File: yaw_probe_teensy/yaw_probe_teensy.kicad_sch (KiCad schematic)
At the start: 5 parts, among them J1 Conn_01x04_Female, U1 Teensy4.0, U2 MS4525DO, U3 MS4525DO, U4 SN65HVD230_CAN_Transceiver

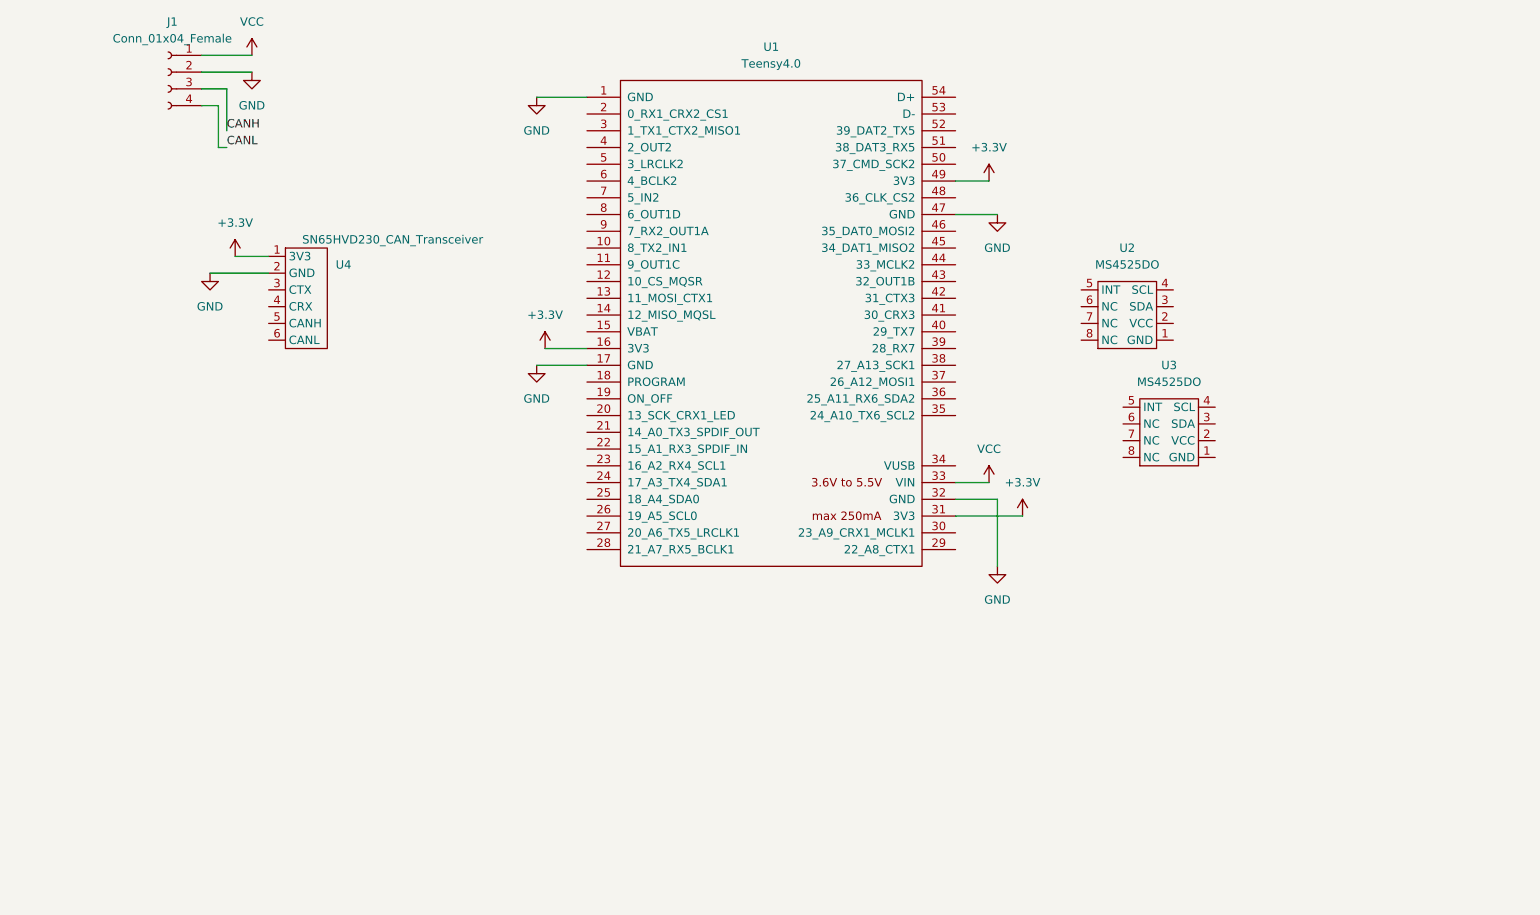
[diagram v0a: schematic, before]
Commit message: yaw probe teensy: schematic finished
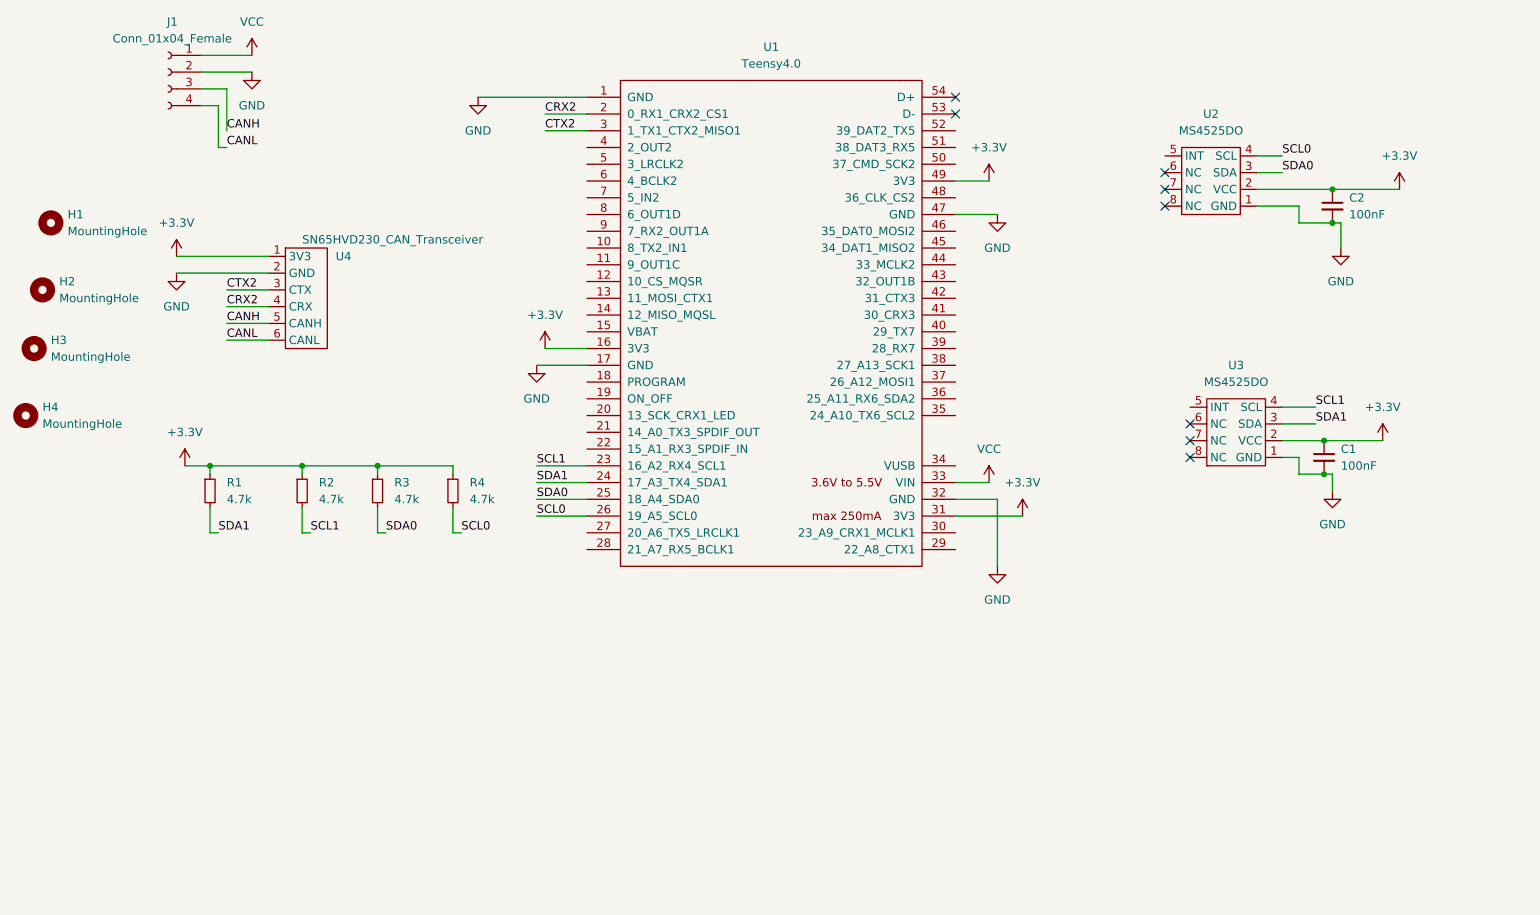
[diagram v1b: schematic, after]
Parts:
- added C1, C2: 100nF, symbol Device:C_Small
- added H1, H2, H3, H4: MountingHole, symbol Mechanical:MountingHole
- added R1, R2, R3, R4: 4.7k, symbol Device:R_Small
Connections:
- net +3.3V: now also U2.2 (VCC), U3.2 (VCC), C1.1, C2.1, R1.1, R2.1, R3.1, R4.1
- net CANH: now also U4.5 (CANH)
- net CANL: now also U4.6 (CANL)
- net GND: now also U2.1 (GND), U3.1 (GND), C1.2, C2.2
- net SDA1: now reaches U3.3 (SDA)
- net SDA1: now also U1.24 (17_A3_TX4_SDA1), R1.2
- net SCL1: now reaches U3.4 (SCL)
- net SCL1: now also U1.23 (16_A2_RX4_SCL1), R2.2
- net CTX2: now reaches U4.3 (CTX)
- net CTX2: now also U1.3 (1_TX1_CTX2_MISO1)
- net CRX2: now reaches U4.4 (CRX)
- net CRX2: now also U1.2 (0_RX1_CRX2_CS1)
- net SDA0: now reaches U1.25 (18_A4_SDA0)
- net SDA0: now also U2.3 (SDA), R3.2
- net SCL0: now reaches U1.26 (19_A5_SCL0)
- net SCL0: now also U2.4 (SCL), R4.2
- no-connect marks 0 -> 8
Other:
- title: SDM-22 Yaw Probe -> SDM-23 Yaw Probe
- moved on the sheet: U2, U3

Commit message: started stm32 variant for yaw probe
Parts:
- H1, H2, H3, H4: footprint (none) -> MountingHole:MountingHole_3.2mm_M3
- J1: footprint (none) -> SDM:Binder_IP40_711_THT_4C
- U1: footprint (none) -> Teensy:Teensy40_SMT
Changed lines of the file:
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@@
       (effects (font (size 1.27 1.27)) (justify left))
     )
-    (property "Footprint" "" (id 2) (at 34.29 96.52 0)
+    (property "Footprint" "MountingHole:MountingHole_3.2mm_M3" (id 2) (at 34.29 96.52 0)
       (effects (font (size 1.27 1.27)) hide)
     )
@@
       (effects (font (size 1.27 1.27)) (justify left))
     )
-    (property "Footprint" "" (id 2) (at 35.56 86.36 0)
+    (property "Footprint" "MountingHole:MountingHole_3.2mm_M3" (id 2) (at 35.56 86.36 0)
       (effects (font (size 1.27 1.27)) hide)
     )
@@
       (effects (font (size 1.27 1.27)) (justify left))
     )
-    (property "Footprint" "" (id 2) (at 38.1 67.31 0)
+    (property "Footprint" "MountingHole:MountingHole_3.2mm_M3" (id 2) (at 38.1 67.31 0)
       (effects (font (size 1.27 1.27)) hide)
     )
@@
       (effects (font (size 1.27 1.27)) (justify left))
     )
-    (property "Footprint" "" (id 2) (at 36.83 77.47 0)
+    (property "Footprint" "MountingHole:MountingHole_3.2mm_M3" (id 2) (at 36.83 77.47 0)
       (effects (font (size 1.27 1.27)) hide)
     )
@@
     (property "Reference" "U1" (id 0) (at 147.32 40.64 0))
     (property "Value" "Teensy4.0" (id 1) (at 147.32 43.18 0))
-    (property "Footprint" "" (id 2) (at 137.16 77.47 0)
+    (property "Footprint" "Teensy:Teensy40_SMT" (id 2) (at 137.16 77.47 0)
       (effects (font (size 1.27 1.27)) hide)
     )
@@
     (property "Reference" "J1" (id 0) (at 56.515 36.83 0))
     (property "Value" "Conn_01x04_Female" (id 1) (at 56.515 39.37 0))
-    (property "Footprint" "" (id 2) (at 55.88 44.45 0)
+    (property "Footprint" "SDM:Binder_IP40_711_THT_4C" (id 2) (at 55.88 44.45 0)
       (effects (font (size 1.27 1.27)) hide)
     )
@@
     )
     (path "/8a11ec2b-d5aa-47fc-b55f-2d7715947a31"
-      (reference "H1") (unit 1) (value "MountingHole") (footprint "")
+      (reference "H1") (unit 1) (value "MountingHole") (footprint "MountingHole:MountingHole_3.2mm_M3")
     )
     (path "/a373a51e-6720-4ebf-be15-7f9cdf4ec4b8"
-      (reference "H2") (unit 1) (value "MountingHole") (footprint "")
+      (reference "H2") (unit 1) (value "MountingHole") (footprint "MountingHole:MountingHole_3.2mm_M3")
     )
     (path "/648b5334-9144-433b-8f9b-4b34383fde3a"
-      (reference "H3") (unit 1) (value "MountingHole") (footprint "")
+      (reference "H3") (unit 1) (value "MountingHole") (footprint "MountingHole:MountingHole_3.2mm_M3")
     )
     (path "/5040622c-3a41-491b-b35b-845caaa0a1f2"
-      (reference "H4") (unit 1) (value "MountingHole") (footprint "")
+      (reference "H4") (unit 1) (value "MountingHole") (footprint "MountingHole:MountingHole_3.2mm_M3")
     )
     (path "/e1059838-0c71-4301-a5b7-3b9d105e9284"
-      (reference "J1") (unit 1) (value "Conn_01x04_Female") (footprint "")
+      (reference "J1") (unit 1) (value "Conn_01x04_Female") (footprint "SDM:Binder_IP40_711_THT_4C")
     )
     (path "/8fca02e5-2732-483b-ad1a-a78a92441fab"
@@
     )
     (path "/b6059556-dcb7-4cd5-903e-0e6be7253ec2"
-      (reference "U1") (unit 1) (value "Teensy4.0") (footprint "")
+      (reference "U1") (unit 1) (value "Teensy4.0") (footprint "Teensy:Teensy40_SMT")
     )
     (path "/e78ea3f6-7e86-4790-9de6-8dee68503fda"

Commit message: imu box
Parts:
- C1, C2: footprint (none) -> Capacitor_THT:C_Disc_D3.0mm_W1.6mm_P2.50mm
- J1: footprint SDM:Binder_IP40_711_THT_4C -> TerminalBlock_TE-Connectivity:TerminalBlock_TE_282834-4_1x04_P2.54mm_Horizontal
- R1, R2, R3, R4: footprint (none) -> Resistor_THT:R_Axial_DIN0207_L6.3mm_D2.5mm_P7.62mm_Horizontal
- U1: footprint Teensy:Teensy40_SMT -> Teensy:Teensy40
- U2, U3: footprint (none) -> SDM:MS4525-DSvoxxxyP
- U4: footprint (none) -> SDM:SDM_CANBoard_v1
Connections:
- net +3.3V: now also U4.3 (3V3); no longer U1.16 (3V3), U1.49 (3V3), U4.1 (3V3)
- net CTX2: now also U4.1 (CTX); no longer U4.3 (CTX)
- net GND: no longer U1.17 (GND), U1.47 (GND)
- no-connect marks 8 -> 52
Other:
- company: Sun Devil Motorsports - Data Acquisition -> Sun Devil Motorsports
- moved on the sheet: H1, H2, H3, H4, R1, R2, R3, R4

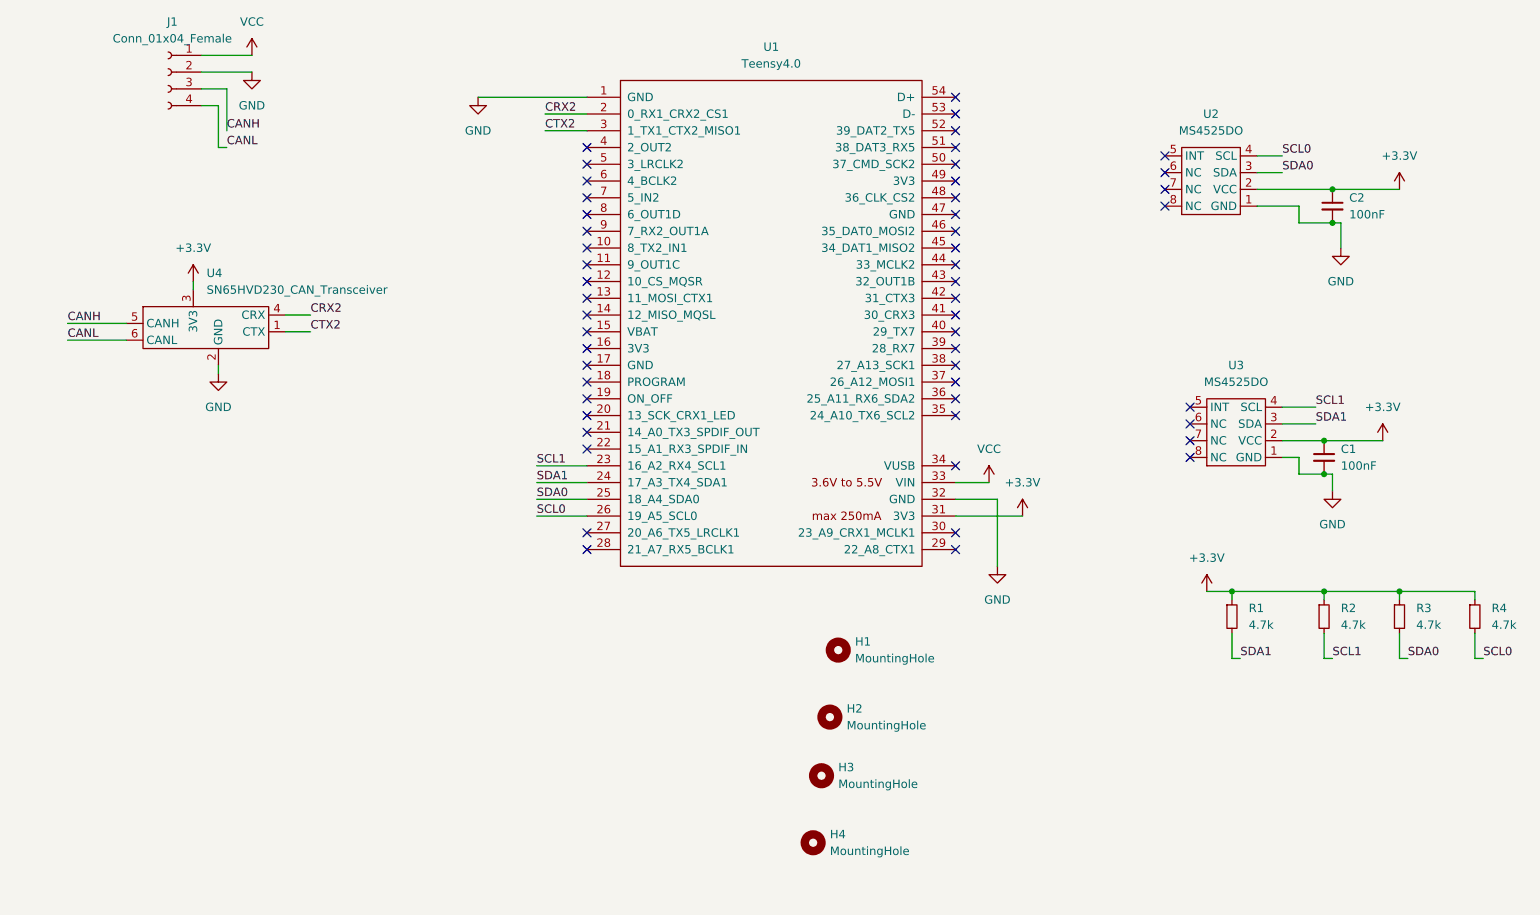
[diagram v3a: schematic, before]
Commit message: update yaw probe for DRS
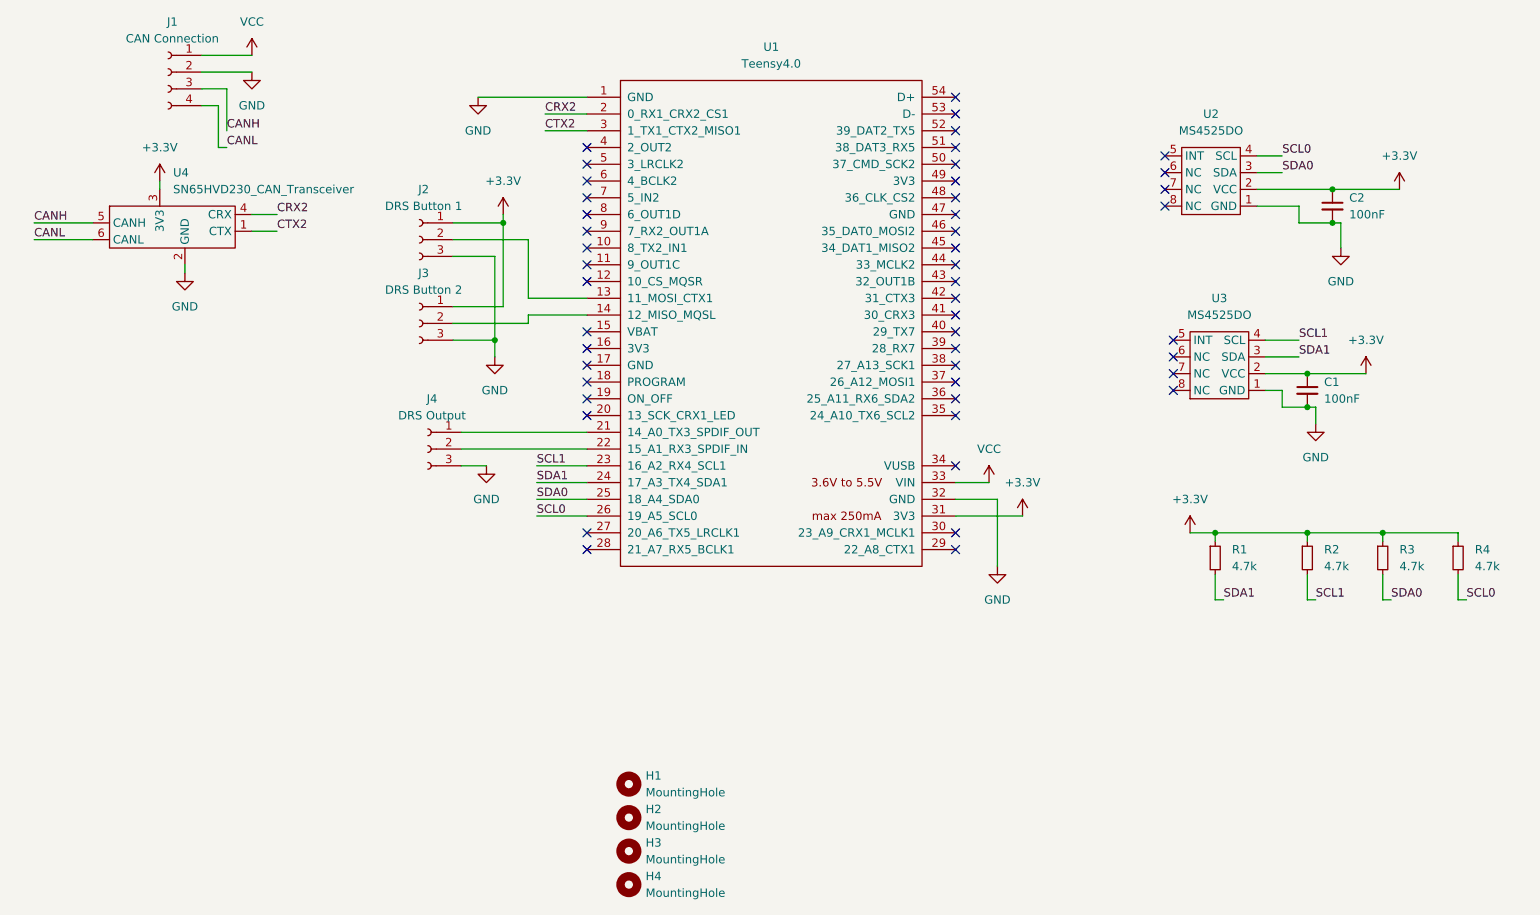
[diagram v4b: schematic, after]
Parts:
- added J2: DRS Button 1, TerminalBlock_TE-Connectivity:TerminalBlock_TE_282834-3_1x03_P2.54mm_Horizontal, symbol Connector:Conn_01x03_Female
- added J3: DRS Button 2, TerminalBlock_TE-Connectivity:TerminalBlock_TE_282834-3_1x03_P2.54mm_Horizontal, symbol Connector:Conn_01x03_Female
- added J4: DRS Output, TerminalBlock_TE-Connectivity:TerminalBlock_TE_282834-3_1x03_P2.54mm_Horizontal, symbol Connector:Conn_01x03_Female
- J1: value Conn_01x04_Female -> CAN Connection
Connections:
- net +3.3V: now also J2.1 (Pin_1), J3.1 (Pin_1)
- net GND: now also J2.3 (Pin_3), J3.3 (Pin_3), J4.3 (Pin_3)
- net at U1.13 (11_MOSI_CTX1): now also J2.2 (Pin_2)
- net at U1.14 (12_MISO_MQSL): now also J3.2 (Pin_2)
- net at U1.21 (14_A0_TX3_SPDIF_OUT): now also J4.1 (Pin_1)
- net at U1.22 (15_A1_RX3_SPDIF_IN): now also J4.2 (Pin_2)
- no-connect marks 52 -> 48
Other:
- moved on the sheet: C1, H1, H2, H3, H4, R1, R2, R3, R4, U3, U4

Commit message: silkscreen additions
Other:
- title: SDM-23 Yaw Probe -> SDM-23 Aero Board
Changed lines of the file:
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@@
   (paper "USLetter")
   (title_block
-    (title "SDM-23 Yaw Probe")
-    (date "2023-01-10")
+    (title "SDM-23 Aero Board")
+    (date "2023-01-11")
     (rev "v1")
     (company "Sun Devil Motorsports")
